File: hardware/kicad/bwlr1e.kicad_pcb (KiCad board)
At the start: 2 copper layers, 36.8 x 90.9 mm, 72 parts, among them Q1 AO3407, Q2 DMG1012UW, SW3 RESET, SW4 BOOT, U1 BME680, U2 RAK3172, U3 AEM10941-QFN, U4 XC6215

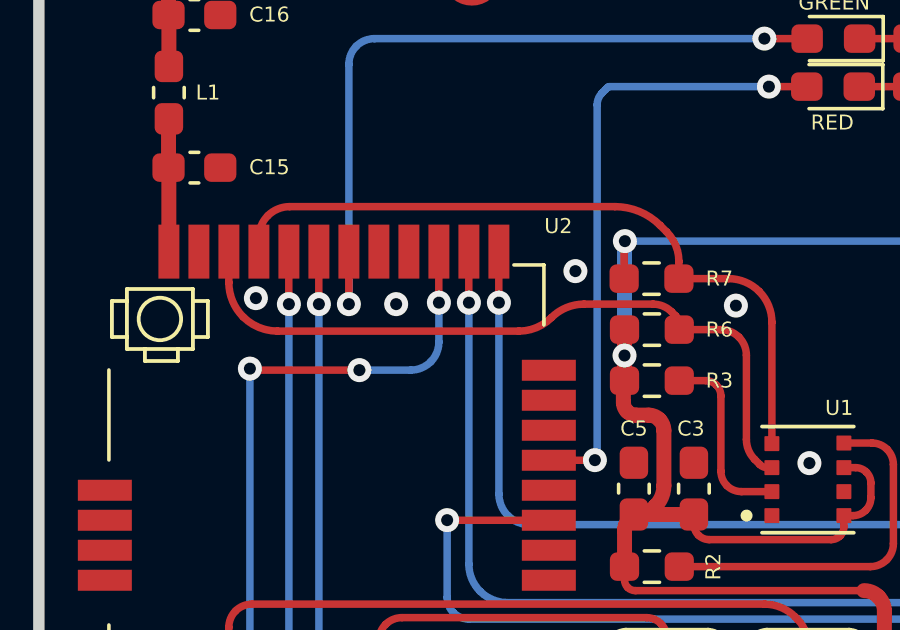
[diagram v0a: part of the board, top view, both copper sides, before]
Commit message: move battery measurement to PB3
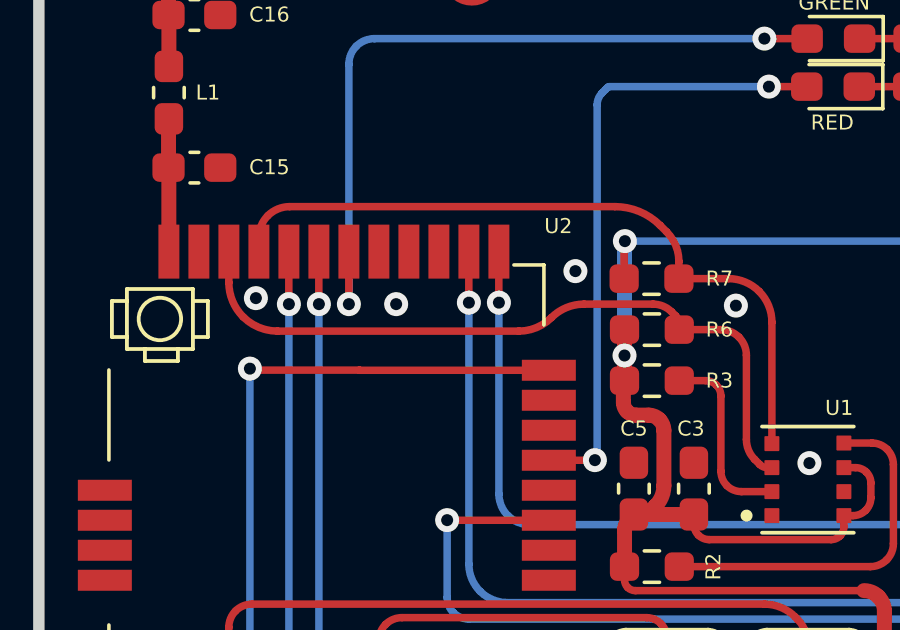
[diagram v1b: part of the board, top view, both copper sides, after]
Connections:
- U2 pad 3: /BATT_MEAS -> unconnected-(U2-Pad3)
- U2 pad 32: unconnected-(U2-Pad32) -> /BATT_MEAS
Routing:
- net /BATT_MEAS: track 39.9 -> 40.0 mm, vias 4 -> 2
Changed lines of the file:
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@@
   (net 29 "unconnected-(U2-Pad30)")
   (net 30 "unconnected-(U2-Pad31)")
-  (net 31 "unconnected-(U2-Pad32)")
+  (net 31 "unconnected-(U2-Pad3)")
   (net 32 "Net-(C16-Pad2)")
   (net 33 "Net-(C7-Pad1)")
@@
       (net 10 "/TXD2") (pinfunction "UART2_TX/PA2") (pintype "bidirectional"))
     (pad "3" smd rect (at 11.5 -14.945 90) (size 1.8 0.7) (layers "F.Cu" "F.Paste" "F.Mask")
-      (net 17 "/BATT_MEAS") (pinfunction "PA15/ADC5") (pintype "bidirectional"))
+      (net 31 "unconnected-(U2-Pad3)") (pinfunction "PA15/ADC5") (pintype "bidirectional+no_connect"))
     (pad "4" smd rect (at 10.5 -14.945 90) (size 1.8 0.7) (layers "F.Cu" "F.Paste" "F.Mask")
       (net 18 "unconnected-(U2-Pad4)") (pinfunction "UART1_TX/PB6") (pintype "bidirectional+no_connect"))
@@
       (net 30 "unconnected-(U2-Pad31)") (pinfunction "PB4/ADC2") (pintype "bidirectional+no_connect"))
     (pad "32" smd rect (at 15.165 -10.99 180) (size 1.8 0.7) (layers "F.Cu" "F.Paste" "F.Mask")
-      (net 31 "unconnected-(U2-Pad32)") (pinfunction "PB3/ADC1") (pintype "bidirectional+no_connect"))
+      (net 17 "/BATT_MEAS") (pinfunction "PB3/ADC1") (pintype "bidirectional"))
     (model "${TEAPOT_3DMODEL_DIR}/RAK3172.STEP"
       (offset (xyz 15.5 0 1))
@@
   (arc (start 142.781801 94.15) (mid 143.075778 94.208475) (end 143.325 94.375) (width 0.25) (layer "F.Cu") (net 16))
   (arc (start 140.57375 94.02375) (mid 140.71359 94.117188) (end 140.878544 94.15) (width 0.25) (layer "F.Cu") (net 16))
+  (segment (start 138.805 81.455) (end 145.115 81.455) (width 0.25) (layer "F.Cu") (net 17))
   (segment (start 135.2875 109.921338) (end 135.2875 111.4) (width 1) (layer "F.Cu") (net 17))
+  (segment (start 138.8 81.45) (end 138.805 81.455) (width 0.25) (layer "F.Cu") (net 17))
   (segment (start 135.235355 81.45) (end 138.8 81.45) (width 0.25) (layer "F.Cu") (net 17))
   (segment (start 135.30625 108.36875) (end 135.24375 108.30625) (width 0.25) (layer "F.Cu") (net 17))
   (segment (start 135.15 108.079917) (end 135.15 107.05) (width 0.25) (layer "F.Cu") (net 17))
   (segment (start 135.175 81.425) (end 135.15 81.4) (width 0.25) (layer "F.Cu") (net 17))
-  (segment (start 141.45 79.2) (end 141.44875 79.19875) (width 0.25) (layer "F.Cu") (net 17))
   (segment (start 135.275 109.891161) (end 135.275 108.506694) (width 1) (layer "F.Cu") (net 17))
-  (segment (start 141.4475 79.195732) (end 141.4475 77.5) (width 0.25) (layer "F.Cu") (net 17))
   (via (at 135.15 81.4) (size 0.8) (drill 0.4) (layers "F.Cu" "B.Cu") (net 17))
   (via (at 135.15 107.05) (size 0.8) (drill 0.4) (layers "F.Cu" "B.Cu") (net 17))
-  (via (at 138.8 81.45) (size 0.8) (drill 0.4) (layers "F.Cu" "B.Cu") (net 17))
-  (via (at 141.45 79.2) (size 0.8) (drill 0.4) (layers "F.Cu" "B.Cu") (net 17))
   (arc (start 135.15 108.079917) (mid 135.174364 108.202407) (end 135.24375 108.30625) (width 0.25) (layer "F.Cu") (net 17))
   (arc (start 135.235355 81.45) (mid 135.202691 81.443502) (end 135.175 81.425) (width 0.25) (layer "F.Cu") (net 17))
@@
   (arc (start 135.275 108.506694) (mid 135.283121 108.465864) (end 135.30625 108.43125) (width 1) (layer "F.Cu") (net 17))
   (arc (start 135.30625 108.36875) (mid 135.319194 108.4) (end 135.30625 108.43125) (width 0.25) (layer "F.Cu") (net 17))
-  (arc (start 141.4475 79.195732) (mid 141.447824 79.197365) (end 141.44875 79.19875) (width 0.25) (layer "F.Cu") (net 17))
   (arc (start 135.275 109.891161) (mid 135.276624 109.899327) (end 135.28125 109.90625) (width 1) (layer "F.Cu") (net 17))
-  (segment (start 140.511091 81.45) (end 138.8 81.45) (width 0.25) (layer "B.Cu") (net 17))
   (segment (start 135.15 107.05) (end 135.15 81.4) (width 0.25) (layer "B.Cu") (net 17))
-  (segment (start 141.45 79.2) (end 141.45 80.511091) (width 0.25) (layer "B.Cu") (net 17))
-  (arc (start 140.511091 81.45) (mid 140.870396 81.378529) (end 141.175 81.175) (width 0.25) (layer "B.Cu") (net 17))
-  (arc (start 141.175 81.175) (mid 141.378529 80.870396) (end 141.45 80.511091) (width 0.25) (layer "B.Cu") (net 17))
   (segment (start 157.075 72) (end 155.4625 72) (width 0.25) (layer "F.Cu") (net 20))
   (segment (start 147.625 77.192677) (end 147.625 78.4) (width 0.25) (layer "F.Cu") (net 27))

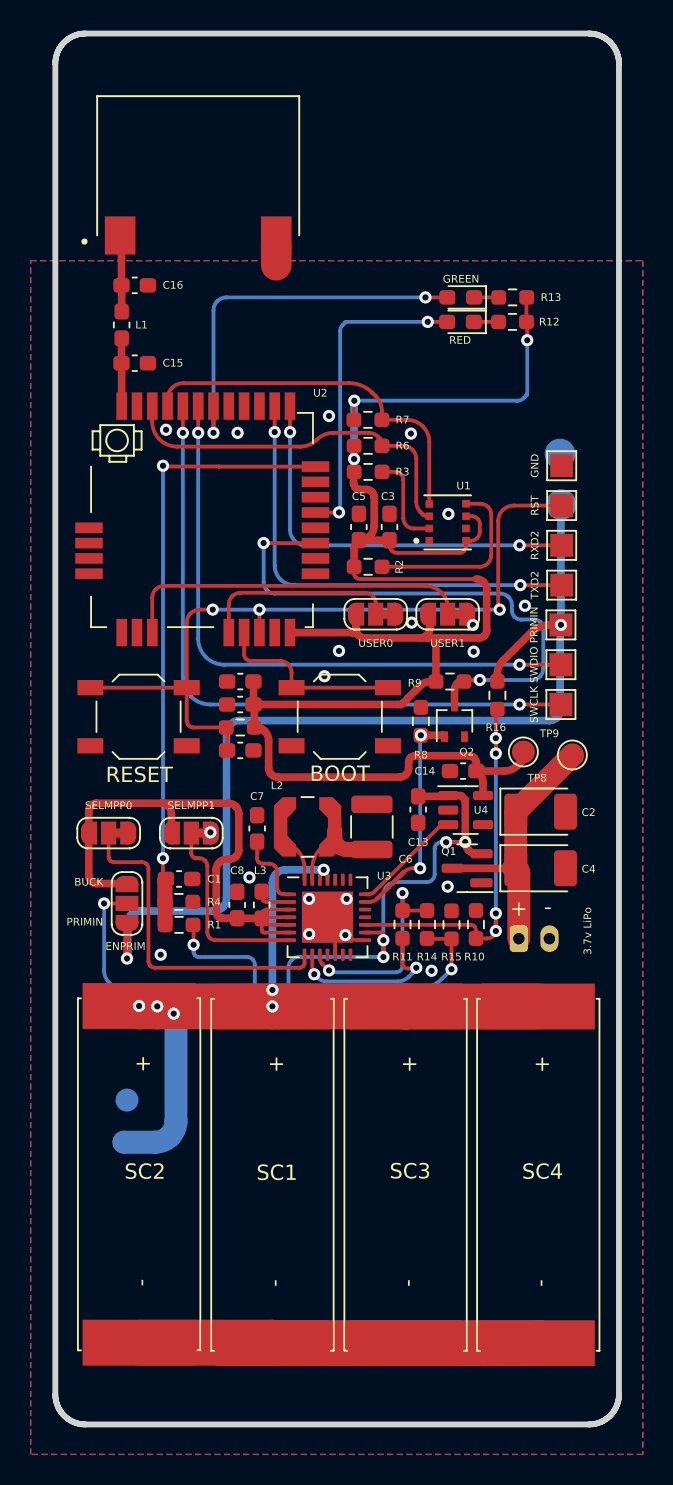
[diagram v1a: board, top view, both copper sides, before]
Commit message: change jst type to smt
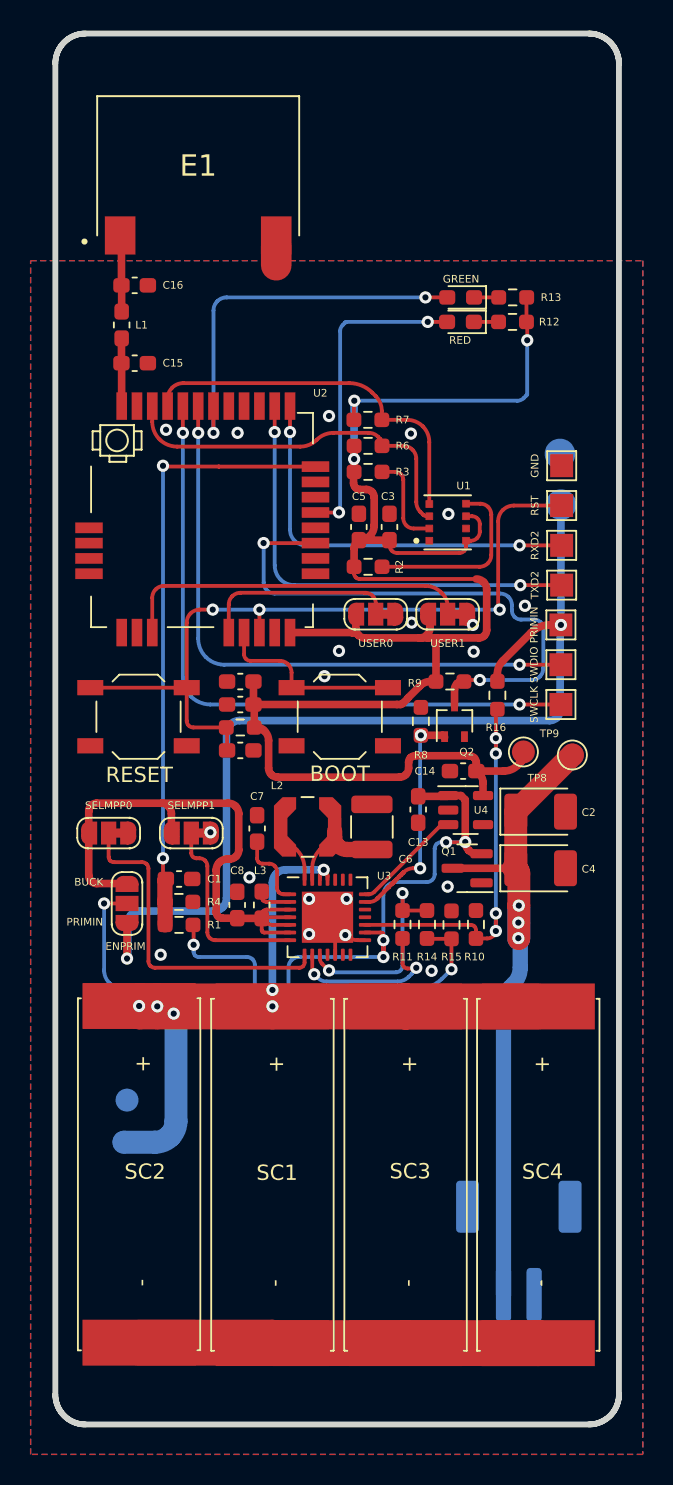
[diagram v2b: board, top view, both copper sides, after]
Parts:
- BT1: footprint Connector_JST:JST_PH_S2B-PH-K_1x02_P2.00mm_Horizontal -> Connector_JST:JST_PH_S2B-PH-SM4-TB_1x02-1MP_P2.00mm_Horizontal
- moved BT1 20.4 mm to (158.4, 132.7)
- moved G*** 5.72 mm to (141.6, 130.2)
- moved G*** 5.72 mm to (137.2, 135.7)
- moved G*** 5.72 mm to (145.2, 136.1)
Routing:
- net Net-(BT1-Pad1): track 18.0 -> 43.7 mm, vias 0 -> 3

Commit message: improve layout and silkscreen info
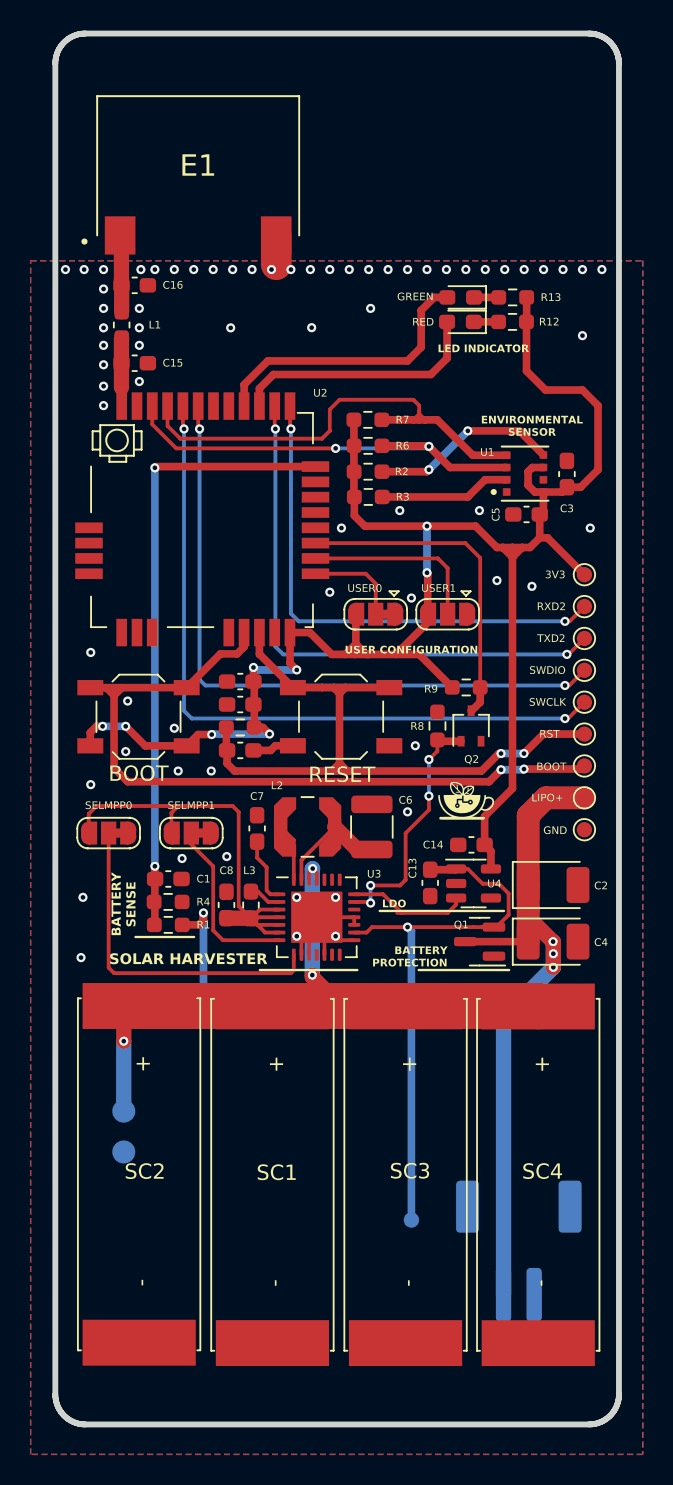
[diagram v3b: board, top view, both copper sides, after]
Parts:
- removed the G*** at (137.2, 135.7)
- removed the G*** at (145.2, 136.1)
- removed JP5: FB_PRIM_EN, Jumper:SolderJumper-3_P1.3mm_Open_RoundedPad1.0x1.5mm_NumberLabels
- removed R10, R15: 1M, Resistor_SMD:R_0603_1608Metric_Pad0.98x0.95mm_HandSolder
- removed R11: 100K, Resistor_SMD:R_0603_1608Metric_Pad0.98x0.95mm_HandSolder
- removed R14: 400K, Resistor_SMD:R_0603_1608Metric_Pad0.98x0.95mm_HandSolder
- removed R16: 0, Resistor_SMD:R_0603_1608Metric_Pad0.98x0.95mm_HandSolder
- removed TP12: PRIMIN, TestPoint:TestPoint_Pad_D2.0mm
- removed TP13: GND, TestPoint:TestPoint_Pad_D2.0mm
- added G***: LOGO, Teapot:TeapotLogo4mm, F.Cu at (154.9, 103.3)
- added TP14: BOOT, TestPoint:TestPoint_Pad_D1.0mm, F.Cu at (162.7, 101.0)
- C1, C11, C12, C3, C5: value 100nF -> 100n
- C13, C14, C17, C8: value 10uF -> 10u
- C6: value 150uF -> 150u
- C7: value 22uF -> 22u
- JP1: footprint Jumper:SolderJumper-3_P1.3mm_Bridged12_RoundedPad1.0x1.5mm_NumberLabels -> Jumper:SolderJumper-3_P1.3mm_Bridged12_RoundedPad1.0x1.5mm
- JP2: footprint Jumper:SolderJumper-3_P1.3mm_Bridged12_RoundedPad1.0x1.5mm_NumberLabels -> Jumper:SolderJumper-3_P1.3mm_Open_RoundedPad1.0x1.5mm
- L3: value 10uH -> 10u
- TP1: value PRIMIN -> LIPO+; footprint TestPoint:TestPoint_Pad_1.5x1.5mm -> TestPoint:TestPoint_Pad_D1.0mm
- TP2, TP3, TP4, TP5, TP6, TP7: footprint TestPoint:TestPoint_Pad_1.5x1.5mm -> TestPoint:TestPoint_Pad_D1.0mm
- TP8: footprint TestPoint:TestPoint_Pad_D1.5mm -> TestPoint:TestPoint_Pad_D1.0mm
- TP9: footprint TestPoint:TestPoint_Pad_D1.5mm -> TestPoint:TestPoint_Pad_D1.0mm; moved to B.Cu
- U1: value BME680 -> BME688
- moved TP9 32.2 mm to (151.4, 130.7), turned to 180 degrees
- moved TP7 23.8 mm to (162.7, 105.2)
- moved TP5 15.0 mm to (162.7, 98.9)
- moved SW3 13.2 mm to (146.8, 97.8)
- moved SW4 13.1 mm to (133.6, 97.8)
- moved TP8 12.2 mm to (162.7, 88.5), turned to 0 degrees
- moved C3 12.1 mm to (161.5, 81.9)
- moved TP1 11.4 mm to (162.7, 103.1), turned to -90 degrees
- moved C5 11.0 mm to (158.9, 84.6), turned to 0 degrees
- moved R2 6.21 mm to (148.6, 81.8)
- moved U1 5.98 mm to (158.8, 81.9)
- moved C2 4.86 mm to (160.6, 108.8)
- moved C4 4.86 mm to (160.6, 112.5)
- moved Q1 4.86 mm to (155.8, 112.5)
- moved C13 4.86 mm to (152.6, 108.7)
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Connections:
- net Net-(C16-Pad2) renamed /ANT
- net Net-(SW4-Pad1) renamed /BOOT
- BT1 pad 1: Net-(BT1-Pad1) -> /LIPO+
- C2 pad 1: Net-(BT1-Pad1) -> /LIPO+
- C4 pad 1: Net-(BT1-Pad1) -> /LIPO+
- Q1 pad 3: Net-(BT1-Pad1) -> /LIPO+
- SW4 pad 2: GND -> +3V3
- TP1 pad 1: /PRIMIN -> /LIPO+
- TP9 pad 1: Net-(BT1-Pad1) -> /BATT+
- U2 pad 19: /USER1 -> unconnected-(U2-PA8-Pad19)
- U2 pad 20: /USER0 -> unconnected-(U2-PA9-Pad20)
- U2 pad 25: unconnected-(U2-Pad25) -> /USER0
- U2 pad 26: unconnected-(U2-Pad26) -> /USER1
- U2 pad 29: /LED1 -> unconnected-(U2-PA0-Pad29)
- U2 pad 3: unconnected-(U2-Pad3) -> /LED1
- U2 pad 4: unconnected-(U2-Pad4) -> /LED2
- U2 pad 6: /LED2 -> unconnected-(U2-PA1-Pad6)
- U3 pad 10: /FB_PRIM_U -> GND
- U3 pad 17: /PRIM -> GND
- U3 pad 9: /FB_PRIM_D -> GND
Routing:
- net /PRIMIN: track 65.0 -> 0.00 mm, vias 2 -> 0
- net /LIPO+: track 0.00 -> 45.4 mm, vias 0 -> 3
- net Net-(BT1-Pad1): track 43.7 -> 0.00 mm, vias 3 -> 0
- net /BOOT: track 12.5 -> 49.8 mm, vias 0 -> 2
- net Net-(JP5-Pad2): track 37.0 -> 0.00 mm, vias 2 -> 0
- net /PRIM: track 26.2 -> 0.00 mm, vias 4 -> 0
- net /BATT+: track 45.1 -> 60.3 mm, vias 5 -> 2
- net Net-(Q2-D): track 36.3 -> 21.4 mm, vias 2 -> 0
- net /FB_PRIM_U: track 13.8 -> 0.00 mm, vias 2 -> 0
- net GND: track 32.3 -> 19.1 mm, vias 20 -> 68
- net /USER1: track 23.2 -> 11.9 mm
- net /FB_PRIM_D: track 11.2 -> 0.00 mm, vias 2 -> 0
- net /BUCK: track 39.2 -> 30.5 mm
- net /LED2: track 25.5 -> 18.4 mm, vias 2 -> 0
- net /RXD2: track 26.4 -> 33.4 mm
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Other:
- board text added: "BATTERY PROTECTION"
- board text added: "BATTERY SENSE"
- board text added: "BWLR1E"
- board text added: "ENVIRONMENTAL SENSOR"
- board text added: "LDO"
- board text added: "LED INDICATOR"
- board text added: "Revision 4"
- board text added: "SOLAR HARVESTER"
- board text added: "Teapotlabs"
- board text added: "USER CONFIGURATION"
- board text removed: "BUCK"
- board text removed: "ENPRIM"
- board text removed: "PRIMIN"

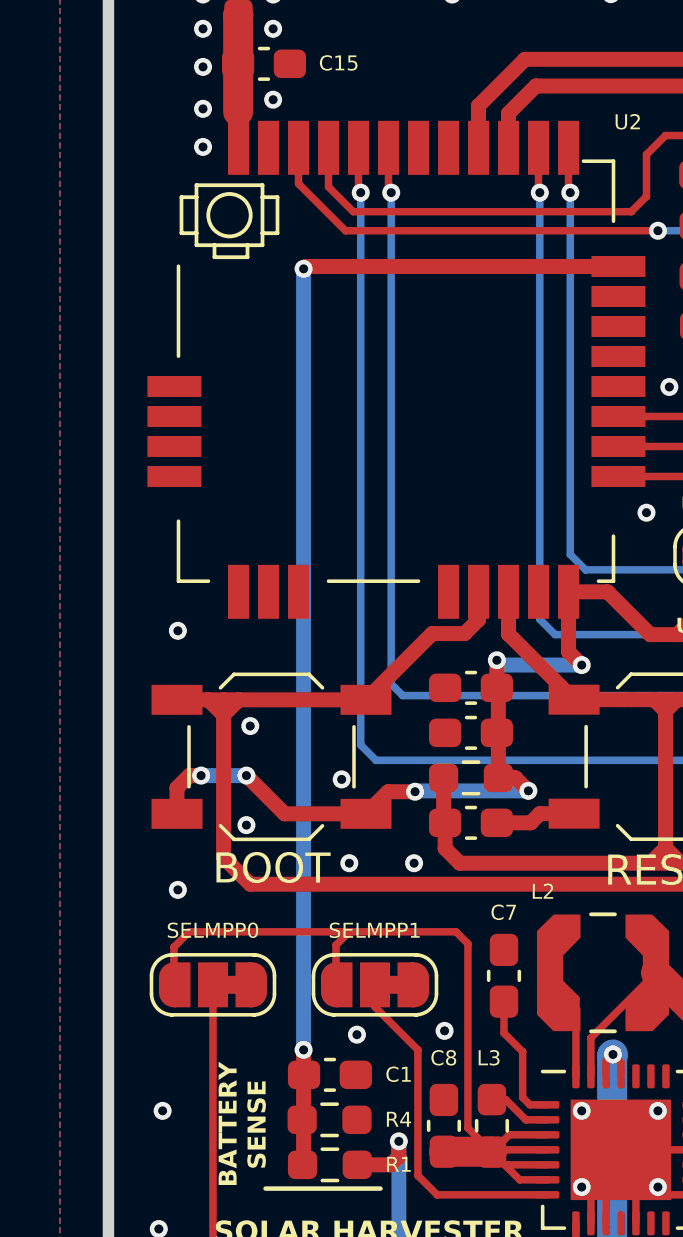
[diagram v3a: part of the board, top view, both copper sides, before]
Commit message: added qwiic connector
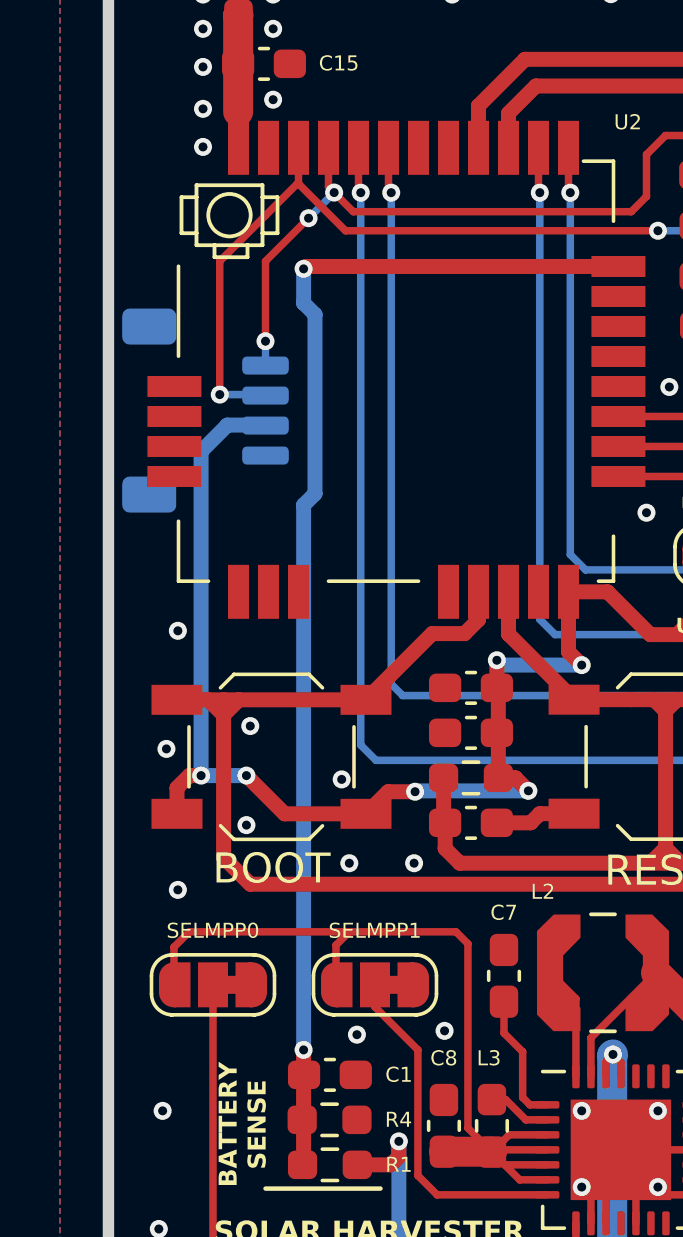
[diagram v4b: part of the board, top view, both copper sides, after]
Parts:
- added J1: Qwiic, Connector_JST:JST_SH_SM04B-SRSS-TB_1x04-1MP_P1.00mm_Horizontal, B.Cu at (131.3, 86.3)
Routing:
- net +3V3: track 122.5 -> 135.9 mm
- net /SDA: track 28.7 -> 38.4 mm, vias 2 -> 3
- net /SCL: track 31.4 -> 38.1 mm, vias 0 -> 3
- net GND: vias 68 -> 69
